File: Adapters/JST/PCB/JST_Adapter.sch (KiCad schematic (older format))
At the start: 8 parts, among them J1 S4B-PH-SM4-TB(LF)(SN), J2 S6B-PH-SM4-TB(LF)(SN), P1 CONN_02X08

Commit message: adapter finished
finished adapter
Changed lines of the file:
@@
 Text Label 3650 3100 0    60   ~ 0
 SPI2_MOSI
-Text Label 2100 3100 0    60   ~ 0
+Text Label 2200 3100 0    60   ~ 0
 SPI2_MISO
-Text Label 2100 3000 0    60   ~ 0
+Text Label 2200 3000 0    60   ~ 0
 SPI2_NSS
 Text Label 2300 3500 0    60   ~ 0

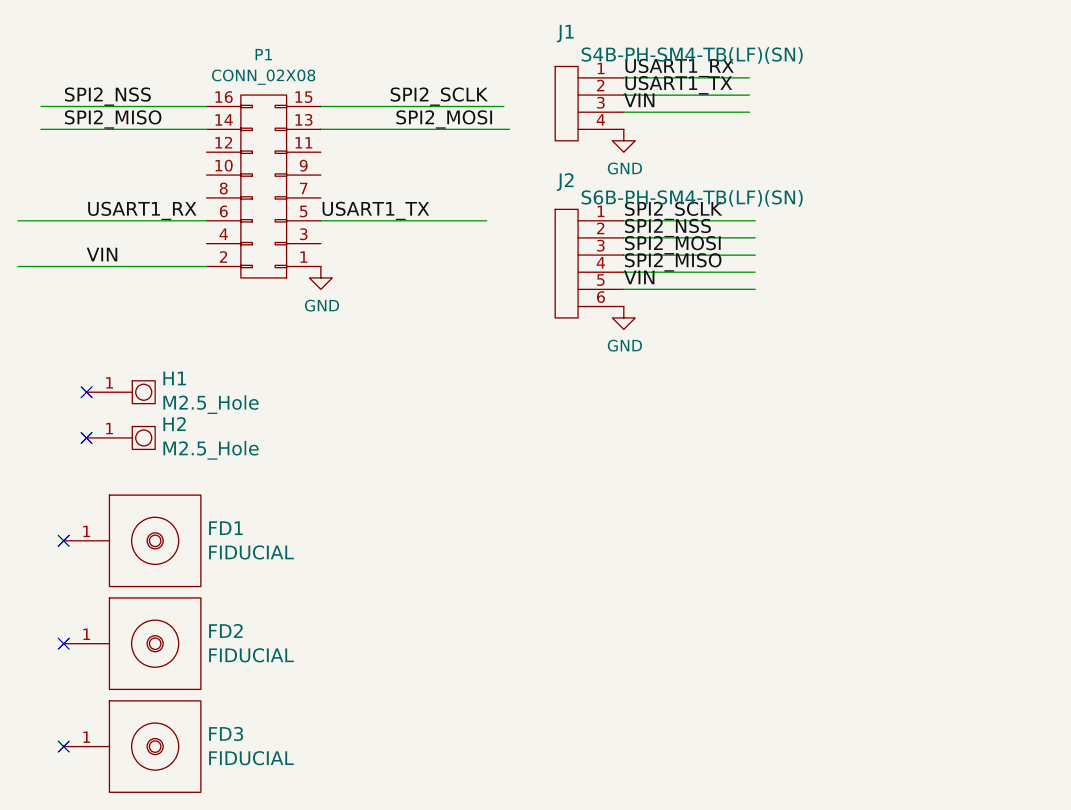
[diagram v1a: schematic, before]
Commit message: Adapters
Adapter ended up being too large. So I split it into two separate
adapters one for SPI and one for USART over JST connectors. SPI board
has 100 ohm inline resistors for EMI and impedance matching in case the
driving device lacks these internally or on its board.  Additional
Fudicials added to the combined implementation.
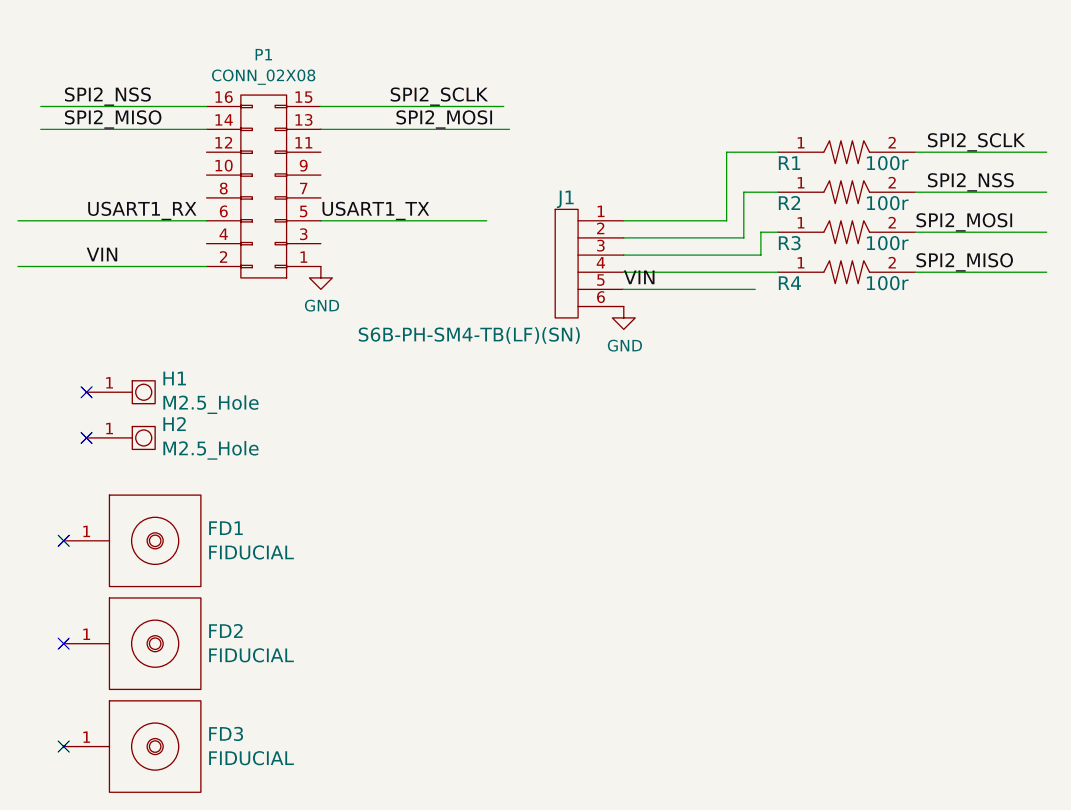
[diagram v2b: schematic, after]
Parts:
- removed J1: S4B-PH-SM4-TB(LF)(SN), PCB_Footprints:S4B-PH-SM4-TB(LF)(SN), symbol S4B-PH-SM4-TB(LF)(SN)
- added R1, R2, R3, R4: TNPW0402100RBEED, PCB_Footprints:R0402, symbol TNPW0402100RBEED
- renumbered J2 to J1
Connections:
- wire segments 15 -> 22
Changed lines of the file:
@@
 $EndComp
 $Comp
-L S6B-PH-SM4-TB(LF)(SN) J2
+L S6B-PH-SM4-TB(LF)(SN) J1
 U 1 1 58296331
 P 4450 3575
-F 0 "J2" H 4400 3825 60  0000 C CNN
-F 1 "S6B-PH-SM4-TB(LF)(SN)" H 4950 3750 60  0000 C CNN
+F 0 "J1" H 4400 3750 60  0000 C CNN
+F 1 "S6B-PH-SM4-TB(LF)(SN)" H 3975 3150 60  0000 C CNN
 F 2 "PCB_Footprints:S6B-PH-SM4-TB(LF)(SN)" H 4300 3650 60  0001 C CNN
 F 3 "http://www.jst-mfg.com/product/pdf/eng/ePH.pdf" H 4175 3950 60  0001 C CNN
@@
 	1    0    0    -1
 $EndComp
-$Comp
-L S4B-PH-SM4-TB(LF)(SN) J1
-U 1 1 582963F6
-P 4450 2950
-F 0 "J1" H 4400 3225 60  0000 C CNN
-F 1 "S4B-PH-SM4-TB(LF)(SN)" H 4950 3125 60  0000 C CNN
-F 2 "PCB_Footprints:S4B-PH-SM4-TB(LF)(SN)" H 4300 3025 60  0001 C CNN
-F 3 "http://www.jst-mfg.com/product/pdf/eng/ePH.pdf" H 4175 3325 60  0001 C CNN
-F 4 "0.32612 @ 5000" H 4275 3425 60  0001 C CNN "Cost"
-F 5 "9 Sept 2016" H 4375 3525 60  0001 C CNN "Date Created "
-F 6 "9 Sept 2016" H 4475 3625 60  0001 C CNN "Date Modified"
-F 7 "Adam Vadala-Roth" H 4575 3725 60  0001 C CNN "Designer "
-F 8 "8mm" H 4675 3825 60  0001 C CNN "Height"
-F 9 "Yes" H 4775 3925 60  0001 C CNN "RHoS?"
-F 10 "JST Sales America Inc" H 4875 4025 60  0001 C CNN "MFR"
-F 11 "S4B-PH-SM4-TB(LF)(SN)" H 4975 4125 60  0001 C CNN "MFR#"
-F 12 "SMT/SMD" H 5075 4225 60  0001 C CNN "Mounting"
-F 13 "4" H 5175 4325 60  0001 C CNN "Pin Count#"
-F 14 "Active" H 5275 4425 60  0001 C CNN "Status"
-F 15 "N/A" H 5375 4525 60  0001 C CNN "Tolerance"
-F 16 "Surface Mount Right angle 4 pin connector" H 5475 4625 60  0001 C CNN "Type"
-F 17 "N/A" H 5575 4725 60  0001 C CNN "Voltage"
-F 18 "N/A" H 5675 4825 60  0001 C CNN "Wattage"
-F 19 "N/A" H 5775 4925 60  0001 C CNN "Component-Value"
-F 20 "4 Positions Header, Shrouded Connector 0.079\" (2.00mm) Through Hole Tin" H 5875 5025 60  0001 C CNN "Description"
-	1    4450 2950
-	1    0    0    -1
-$EndComp
 Text Label 3625 3000 0    60   ~ 0
 SPI2_SCLK
@@
 Wire Wire Line
 	2000 3700 2825 3700
-Text Label 4650 2875 0    60   ~ 0
-USART1_RX
-Text Label 4650 2950 0    60   ~ 0
-USART1_TX
-Wire Wire Line
-	5200 2875 4650 2875
-Wire Wire Line
-	5200 2950 4650 2950
-Wire Wire Line
-	5200 3025 4650 3025
 $Comp
 L GND #PWR02
@@
 	1    0    0    -1
 $EndComp
-$Comp
-L GND #PWR03
-U 1 1 58297393
-P 4650 3100
-F 0 "#PWR03" H 4650 2850 50  0001 C CNN
-F 1 "GND" H 4655 2927 50  0000 C CNN
-F 2 "" H 4650 3100 50  0000 C CNN
-F 3 "" H 4650 3100 50  0000 C CNN
-	1    4650 3100
-	1    0    0    -1
-$EndComp
 Text Label 4650 3800 0    60   ~ 0
 VIN
 Wire Wire Line
 	4650 3800 5225 3800
-Text Label 4650 3025 0    60   ~ 0
-VIN
-Text Label 4650 3500 0    60   ~ 0
+Text Label 5975 3200 0    60   ~ 0
 SPI2_SCLK
-Text Label 4650 3575 0    60   ~ 0
+Text Label 5975 3375 0    60   ~ 0
 SPI2_NSS
-Text Label 4650 3650 0    60   ~ 0
+Text Label 5925 3550 0    60   ~ 0
 SPI2_MOSI
-Text Label 4650 3725 0    60   ~ 0
+Text Label 5925 3725 0    60   ~ 0
 SPI2_MISO
 Wire Wire Line
-	5225 3500 4650 3500
-Wire Wire Line
-	5225 3575 4650 3575
-Wire Wire Line
-	5225 3650 4650 3650
-Wire Wire Line
-	5225 3725 4650 3725
+	6500 3200 5925 3200
+Wire Wire Line
+	6500 3375 5925 3375
+Wire Wire Line
+	6500 3550 5925 3550
+Wire Wire Line
+	6500 3725 5925 3725
 $Comp
 L M2.5_Hole H1
@@
 NoConn ~ 2300 4250
 NoConn ~ 2300 4450
+$Comp
+L TNPW0402100RBEED R4
+U 1 1 582B1B9A
+P 5625 3725
+F 0 "R4" H 5375 3675 60  0000 C CNN
+F 1 "TNPW0402100RBEED" H 5625 3972 60  0001 C CNN
+F 2 "PCB_Footprints:R0402" H 5225 3975 60  0001 C CNN
+F 3 "http://www.vishay.com/docs/28758/tnpw_e3.pdf" H 5325 4175 60  0001 C CNN
+F 4 "0.11880 @ 2500" H 7175 5675 60  0001 C CNN "Cost"
+F 5 "14 Nov 2016" H 5525 4275 60  0001 C CNN "Date Created"
+F 6 "14 Nov 2016" H 5625 4375 60  0001 C CNN "Date Modified"
+F 7 "Adam Vadala-Roth" H 5725 4475 60  0001 C CNN "Designer"
+F 8 "0.4mm" H 5825 4575 60  0001 C CNN "Height"
+F 9 "Yes" H 5925 4675 60  0001 C CNN "RHoS?"
+F 10 "Vishay Dale" H 6025 4775 60  0001 C CNN "MFR"
+F 11 "TNPW0402100RBEED" H 6125 4875 60  0001 C CNN "MFR#"
+F 12 "SMT/SMD" H 6225 4975 60  0001 C CNN "Mounting"
+F 13 "2" H 6325 5075 60  0001 C CNN "Pin Count#"
+F 14 "Active" H 6425 5175 60  0001 C CNN "Status"
+F 15 "0.1%" H 6525 5275 60  0001 C CNN "Tolerance"
+F 16 "passive" H 6625 5375 60  0001 C CNN "Type"
+F 17 "N/A" H 6725 5475 60  0001 C CNN "Voltage"
+F 18 "1/16" H 6825 5575 60  0001 C CNN "Wattage"
+F 19 "100r" H 5800 3675 60  0000 C CNN "Component-Value"
+F 20 "RES SMD 100 OHM 0.1% 1/16W 0402" H 7025 5775 60  0001 C CNN "Description"
+	1    5625 3725
+	1    0    0    -1
+$EndComp
+$Comp
+L TNPW0402100RBEED R3
+U 1 1 582B1F74
+P 5625 3550
+F 0 "R3" H 5375 3500 60  0000 C CNN
+F 1 "TNPW0402100RBEED" H 5625 3797 60  0001 C CNN
+F 2 "PCB_Footprints:R0402" H 5225 3800 60  0001 C CNN
+F 3 "http://www.vishay.com/docs/28758/tnpw_e3.pdf" H 5325 4000 60  0001 C CNN
+F 4 "0.11880 @ 2500" H 7175 5500 60  0001 C CNN "Cost"
+F 5 "14 Nov 2016" H 5525 4100 60  0001 C CNN "Date Created"
+F 6 "14 Nov 2016" H 5625 4200 60  0001 C CNN "Date Modified"
+F 7 "Adam Vadala-Roth" H 5725 4300 60  0001 C CNN "Designer"
+F 8 "0.4mm" H 5825 4400 60  0001 C CNN "Height"
+F 9 "Yes" H 5925 4500 60  0001 C CNN "RHoS?"
+F 10 "Vishay Dale" H 6025 4600 60  0001 C CNN "MFR"
+F 11 "TNPW0402100RBEED" H 6125 4700 60  0001 C CNN "MFR#"
+F 12 "SMT/SMD" H 6225 4800 60  0001 C CNN "Mounting"
+F 13 "2" H 6325 4900 60  0001 C CNN "Pin Count#"
+F 14 "Active" H 6425 5000 60  0001 C CNN "Status"
+F 15 "0.1%" H 6525 5100 60  0001 C CNN "Tolerance"
+F 16 "passive" H 6625 5200 60  0001 C CNN "Type"
+F 17 "N/A" H 6725 5300 60  0001 C CNN "Voltage"
+F 18 "1/16" H 6825 5400 60  0001 C CNN "Wattage"
+F 19 "100r" H 5800 3500 60  0000 C CNN "Component-Value"
+F 20 "RES SMD 100 OHM 0.1% 1/16W 0402" H 7025 5600 60  0001 C CNN "Description"
+	1    5625 3550
+	1    0    0    -1
+$EndComp
+$Comp
+L TNPW0402100RBEED R2
+U 1 1 582B209D
+P 5625 3375
+F 0 "R2" H 5375 3325 60  0000 C CNN
+F 1 "TNPW0402100RBEED" H 5625 3622 60  0001 C CNN
+F 2 "PCB_Footprints:R0402" H 5225 3625 60  0001 C CNN
+F 3 "http://www.vishay.com/docs/28758/tnpw_e3.pdf" H 5325 3825 60  0001 C CNN
+F 4 "0.11880 @ 2500" H 7175 5325 60  0001 C CNN "Cost"
+F 5 "14 Nov 2016" H 5525 3925 60  0001 C CNN "Date Created"
+F 6 "14 Nov 2016" H 5625 4025 60  0001 C CNN "Date Modified"
+F 7 "Adam Vadala-Roth" H 5725 4125 60  0001 C CNN "Designer"
+F 8 "0.4mm" H 5825 4225 60  0001 C CNN "Height"
+F 9 "Yes" H 5925 4325 60  0001 C CNN "RHoS?"
+F 10 "Vishay Dale" H 6025 4425 60  0001 C CNN "MFR"
+F 11 "TNPW0402100RBEED" H 6125 4525 60  0001 C CNN "MFR#"
+F 12 "SMT/SMD" H 6225 4625 60  0001 C CNN "Mounting"
+F 13 "2" H 6325 4725 60  0001 C CNN "Pin Count#"
+F 14 "Active" H 6425 4825 60  0001 C CNN "Status"
+F 15 "0.1%" H 6525 4925 60  0001 C CNN "Tolerance"
+F 16 "passive" H 6625 5025 60  0001 C CNN "Type"
+F 17 "N/A" H 6725 5125 60  0001 C CNN "Voltage"
+F 18 "1/16" H 6825 5225 60  0001 C CNN "Wattage"
+F 19 "100r" H 5800 3325 60  0000 C CNN "Component-Value"
+F 20 "RES SMD 100 OHM 0.1% 1/16W 0402" H 7025 5425 60  0001 C CNN "Description"
+	1    5625 3375
+	1    0    0    -1
+$EndComp
+$Comp
+L TNPW0402100RBEED R1
+U 1 1 582B20B4
+P 5625 3200
+F 0 "R1" H 5375 3150 60  0000 C CNN
+F 1 "TNPW0402100RBEED" H 5625 3447 60  0001 C CNN
+F 2 "PCB_Footprints:R0402" H 5225 3450 60  0001 C CNN
+F 3 "http://www.vishay.com/docs/28758/tnpw_e3.pdf" H 5325 3650 60  0001 C CNN
+F 4 "0.11880 @ 2500" H 7175 5150 60  0001 C CNN "Cost"
+F 5 "14 Nov 2016" H 5525 3750 60  0001 C CNN "Date Created"
+F 6 "14 Nov 2016" H 5625 3850 60  0001 C CNN "Date Modified"
+F 7 "Adam Vadala-Roth" H 5725 3950 60  0001 C CNN "Designer"
+F 8 "0.4mm" H 5825 4050 60  0001 C CNN "Height"
+F 9 "Yes" H 5925 4150 60  0001 C CNN "RHoS?"
+F 10 "Vishay Dale" H 6025 4250 60  0001 C CNN "MFR"
+F 11 "TNPW0402100RBEED" H 6125 4350 60  0001 C CNN "MFR#"
+F 12 "SMT/SMD" H 6225 4450 60  0001 C CNN "Mounting"
+F 13 "2" H 6325 4550 60  0001 C CNN "Pin Count#"
+F 14 "Active" H 6425 4650 60  0001 C CNN "Status"
+F 15 "0.1%" H 6525 4750 60  0001 C CNN "Tolerance"
+F 16 "passive" H 6625 4850 60  0001 C CNN "Type"
+F 17 "N/A" H 6725 4950 60  0001 C CNN "Voltage"
+F 18 "1/16" H 6825 5050 60  0001 C CNN "Wattage"
+F 19 "100r" H 5800 3150 60  0000 C CNN "Component-Value"
+F 20 "RES SMD 100 OHM 0.1% 1/16W 0402" H 7025 5250 60  0001 C CNN "Description"
+	1    5625 3200
+	1    0    0    -1
+$EndComp
+Wire Wire Line
+	4650 3725 5325 3725
+Wire Wire Line
+	5325 3550 5250 3550
+Wire Wire Line
+	5250 3550 5250 3650
+Wire Wire Line
+	5250 3650 4650 3650
+Wire Wire Line
+	5325 3375 5175 3375
+Wire Wire Line
+	5175 3375 5175 3575
+Wire Wire Line
+	5175 3575 4650 3575
+Wire Wire Line
+	5325 3200 5100 3200
+Wire Wire Line
+	5100 3200 5100 3500
+Wire Wire Line
+	5100 3500 4650 3500
 $EndSCHEMATC
